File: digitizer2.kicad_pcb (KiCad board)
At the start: 6 copper layers, 4 parts, among them U1 XC7A35T, U2 FT2232H, U3 MT41J128M16, U4 ADS5403

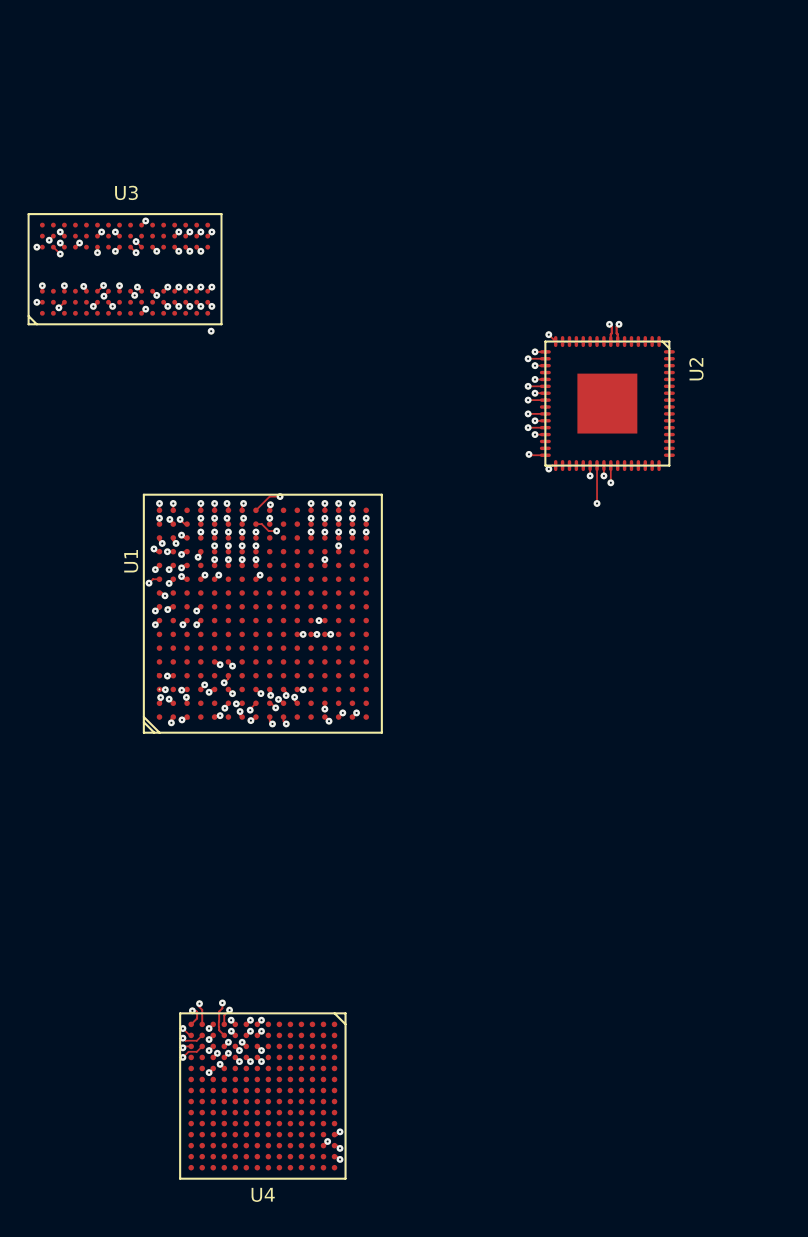
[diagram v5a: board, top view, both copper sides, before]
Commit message: Power supply initial selection
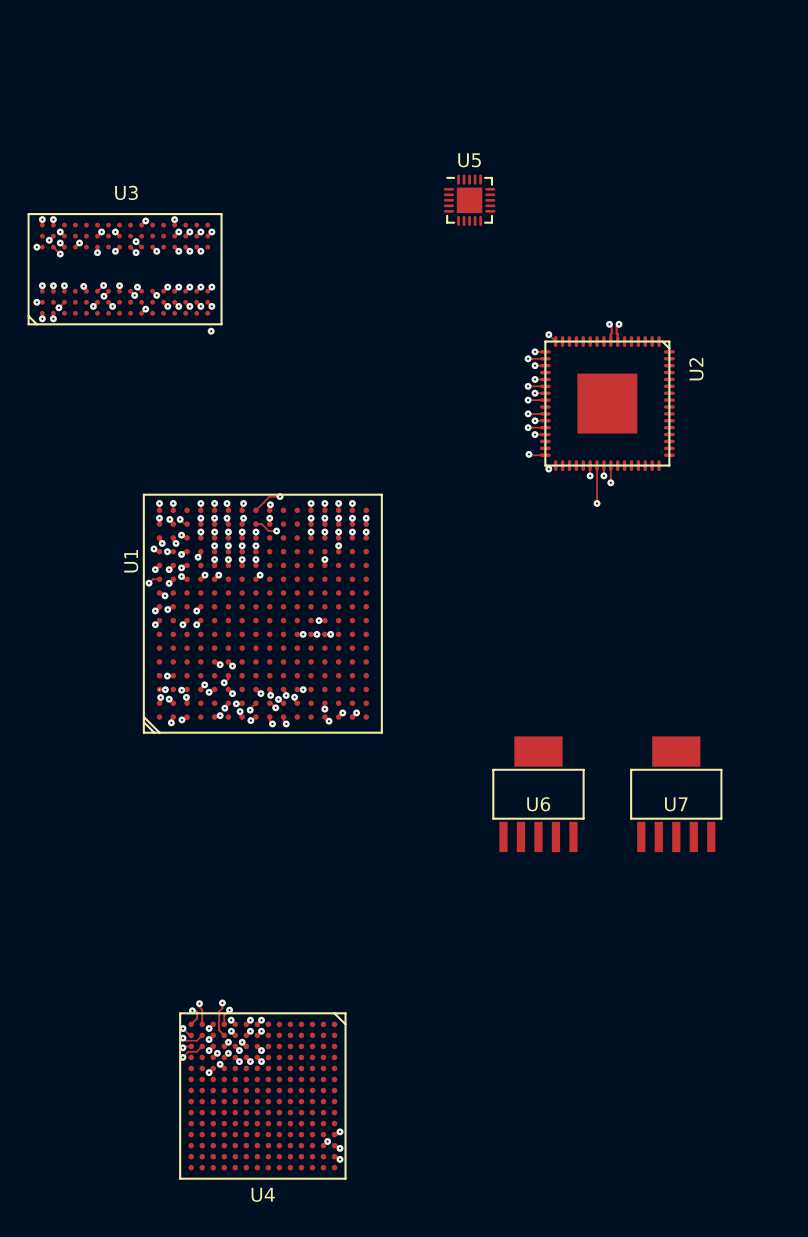
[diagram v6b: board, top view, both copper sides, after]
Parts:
- added U5: LTC3569, Housings_DFN_QFN:UQFN-20-1EP_3x3mm_Pitch0.4mm, F.Cu at (175.0, 65.0)
- added U6: TPS79618DCQ, digitizer2_modules:SOT-223-6, F.Cu at (180.0, 108.1)
- added U7: TPS79633DCQ, digitizer2_modules:SOT-223-6, F.Cu at (190.0, 108.1)
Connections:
- U1 pad A1: Net-(U1-PadA1) -> GND
- U1 pad A11: Net-(U1-PadA11) -> GND
- U1 pad B13: Net-(U1-PadB13) -> Net-(U1-PadA16)
- U1 pad B3: Net-(U1-PadB3) -> Net-(U1-PadA6)
- U1 pad B8: Net-(U1-PadB8) -> GND
- U1 pad C10: Net-(U1-PadC10) -> Net-(U1-PadA16)
- U1 pad C15: Net-(U1-PadC15) -> GND
- U1 pad C5: Net-(U1-PadC5) -> GND
- U1 pad D12: Net-(U1-PadD12) -> GND
- U1 pad D2: Net-(U1-PadD2) -> GND
- U1 pad D7: Net-(U1-PadD7) -> Net-(U1-PadA6)
- U1 pad E14: Net-(U1-PadE14) -> Net-(U1-PadA16)
- U1 pad E4: Net-(U1-PadE4) -> Net-(U1-PadA6)
- U1 pad E9: Net-(U1-PadE9) -> GND
- U1 pad F1: Net-(U1-PadF1) -> Net-(U1-PadA6)
- U1 pad F10: Net-(U1-PadF10) -> GND
- U1 pad F11: Net-(U1-PadF11) -> Net-(U1-PadE10)
- U1 pad F16: Net-(U1-PadF16) -> GND
- U1 pad F6: Net-(U1-PadF6) -> GND
- U1 pad F9: Net-(U1-PadF9) -> Net-(U1-PadF7)
- U1 pad G13: Net-(U1-PadG13) -> GND
- U1 pad G3: Net-(U1-PadG3) -> GND
- U1 pad G6: Net-(U1-PadG6) -> Net-(U1-PadF7)
- U1 pad G9: Net-(U1-PadG9) -> GND
- U1 pad H15: Net-(U1-PadH15) -> Net-(U1-PadA16)
- U1 pad H6: Net-(U1-PadH6) -> GND
- U1 pad H9: Net-(U1-PadH9) -> Net-(U1-PadF7)
- U1 pad J10: Net-(U1-PadJ10) -> Net-(U1-PadG10)
- U1 pad J11: Net-(U1-PadJ11) -> GND
- U1 pad J12: Net-(U1-PadJ12) -> Net-(U1-PadA16)
- U1 pad J2: Net-(U1-PadJ2) -> Net-(U1-PadA6)
- U1 pad J6: Net-(U1-PadJ6) -> Net-(U1-PadF7)
- U1 pad J9: Net-(U1-PadJ9) -> GND
- U1 pad K11: Net-(U1-PadK11) -> Net-(U1-PadG10)
- U1 pad K14: Net-(U1-PadK14) -> GND
- U1 pad K4: Net-(U1-PadK4) -> GND
- U1 pad K6: Net-(U1-PadK6) -> GND
- U1 pad K9: Net-(U1-PadK9) -> Net-(U1-PadF7)
- U1 pad L1: Net-(U1-PadL1) -> GND
- U1 pad L10: Net-(U1-PadL10) -> Net-(U1-PadG10)
- U1 pad L11: Net-(U1-PadL11) -> GND
- U1 pad L8: Net-(U1-PadL8) -> Net-(U1-PadF7)
- U1 pad M13: Net-(U1-PadM13) -> Net-(U1-PadL16)
- U1 pad M8: Net-(U1-PadM8) -> GND
- U1 pad N10: Net-(U1-PadN10) -> Net-(U1-PadL16)
- U1 pad N15: Net-(U1-PadN15) -> GND
- U1 pad N5: Net-(U1-PadN5) -> GND
- U1 pad P12: Net-(U1-PadP12) -> GND
- U1 pad P2: Net-(U1-PadP2) -> GND
- U1 pad P7: Net-(U1-PadP7) -> Net-(U1-PadL16)
- U1 pad R14: Net-(U1-PadR14) -> Net-(U1-PadL16)
- U1 pad R4: Net-(U1-PadR4) -> Net-(U1-PadM3)
- U1 pad R9: Net-(U1-PadR9) -> GND
- U1 pad T1: Net-(U1-PadT1) -> Net-(U1-PadM3)
- U1 pad T11: Net-(U1-PadT11) -> Net-(U1-PadL16)
- U1 pad T16: Net-(U1-PadT16) -> GND
- U1 pad T6: Net-(U1-PadT6) -> GND
- U2 pad 1: Net-(U2-Pad1) -> GND
- U2 pad 10: Net-(U2-Pad1) -> GND
- U2 pad 11: Net-(U2-Pad1) -> GND
- U2 pad 15: Net-(U2-Pad1) -> GND
- U2 pad 25: Net-(U2-Pad1) -> GND
- U2 pad 35: Net-(U2-Pad1) -> GND
- U2 pad 47: Net-(U2-Pad1) -> GND
- U2 pad 5: Net-(U2-Pad1) -> GND
- U2 pad 51: Net-(U2-Pad1) -> GND
- U2 pad PAD: Net-(U2-Pad1) -> GND
- U3 pad A9: Net-(U3-PadA9) -> GND
- U3 pad B1: Net-(U3-PadB1) -> GND
- U3 pad B3: Net-(U3-PadA9) -> GND
- U3 pad B9: Net-(U3-PadB1) -> GND
- U3 pad D1: Net-(U3-PadB1) -> GND
- U3 pad D8: Net-(U3-PadB1) -> GND
- U3 pad E1: Net-(U3-PadA9) -> GND
- U3 pad E2: Net-(U3-PadB1) -> GND
- U3 pad E8: Net-(U3-PadB1) -> GND
- U3 pad F9: Net-(U3-PadB1) -> GND
- U3 pad G1: Net-(U3-PadB1) -> GND
- U3 pad G8: Net-(U3-PadA9) -> GND
- U3 pad G9: Net-(U3-PadB1) -> GND
- U3 pad J2: Net-(U3-PadA9) -> GND
- U3 pad J8: Net-(U3-PadA9) -> GND
- U3 pad M1: Net-(U3-PadA9) -> GND
- U3 pad M9: Net-(U3-PadA9) -> GND
- U3 pad P1: Net-(U3-PadA9) -> GND
- U3 pad P9: Net-(U3-PadA9) -> GND
- U3 pad T1: Net-(U3-PadA9) -> GND
- U3 pad T9: Net-(U3-PadA9) -> GND
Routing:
- net GND: track 0.00 -> 4.60 mm, vias 0 -> 9
- net Net-(U1-PadA16): track 0.50 -> 3.06 mm, vias 1 -> 4
- net Net-(U1-PadH15): track 1.71 -> 0.00 mm, vias 1 -> 0
- net Net-(U1-PadA11): track 0.88 -> 0.00 mm, vias 1 -> 0
- net Net-(U1-PadC15): track 0.64 -> 0.00 mm, vias 1 -> 0
- net Net-(U1-PadJ2): track 0.57 -> 0.00 mm, vias 1 -> 0
- net Net-(U1-PadA6): track 0.00 -> 0.57 mm, vias 0 -> 1
- net Net-(U1-PadF16): track 0.54 -> 0.00 mm, vias 1 -> 0
- net Net-(U1-PadB13): track 0.43 -> 0.00 mm, vias 1 -> 0
- net Net-(U1-PadR14): track 0.43 -> 0.00 mm, vias 1 -> 0
- net Net-(U1-PadL16): track 0.00 -> 0.43 mm, vias 0 -> 1
- net Net-(U1-PadE14): track 0.43 -> 0.00 mm, vias 1 -> 0
- net Net-(U1-PadN15): track 0.43 -> 0.00 mm, vias 1 -> 0
- net Net-(U1-PadG13): track 0.42 -> 0.00 mm, vias 1 -> 0
- net Net-(U3-PadB2): track 0.00 -> 0.40 mm, vias 0 -> 1
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
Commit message: Config bank. Power labels
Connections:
- net Net-(U1-PadK10) renamed /INIT_B
- net Net-(U1-PadL9) renamed /PROGRAM_B
- net Net-(U4-PadD12) renamed /VDD_ADC_3V3
- U1 pad A16: Net-(U1-PadA16) -> /VDD_DRAM_1V5
- U1 pad A6: Net-(U1-PadA6) -> /VDD_ADC_1V8
- U1 pad B13: Net-(U1-PadA16) -> /VDD_DRAM_1V5
- U1 pad B3: Net-(U1-PadA6) -> /VDD_ADC_1V8
- U1 pad C10: Net-(U1-PadA16) -> /VDD_DRAM_1V5
- U1 pad D7: Net-(U1-PadA6) -> /VDD_ADC_1V8
- U1 pad E10: Net-(U1-PadE10) -> /VDD_FPGA_1V0
- U1 pad E14: Net-(U1-PadA16) -> /VDD_DRAM_1V5
- U1 pad E4: Net-(U1-PadA6) -> /VDD_ADC_1V8
- U1 pad E7: Net-(U1-PadE7) -> /VDD_FPGA_3V3
- U1 pad F1: Net-(U1-PadA6) -> /VDD_ADC_1V8
- U1 pad F11: Net-(U1-PadE10) -> /VDD_FPGA_1V0
- U1 pad F7: Net-(U1-PadF7) -> /VDD_FPGA_1V0
- U1 pad F8: Net-(U1-PadF8) -> /VDD_FPGA_1V8
- U1 pad F9: Net-(U1-PadF7) -> /VDD_FPGA_1V0
- U1 pad G10: Net-(U1-PadG10) -> /VDD_FPGA_1V8
- U1 pad G6: Net-(U1-PadF7) -> /VDD_FPGA_1V0
- U1 pad G7: Net-(U1-PadG7) -> GND
- U1 pad G8: Net-(U1-PadG8) -> /VDD_FPGA_1V8
- U1 pad H15: Net-(U1-PadA16) -> /VDD_DRAM_1V5
- U1 pad H7: Net-(U1-PadH7) -> GND
- U1 pad H9: Net-(U1-PadF7) -> /VDD_FPGA_1V0
- U1 pad J10: Net-(U1-PadG10) -> /VDD_FPGA_1V8
- U1 pad J12: Net-(U1-PadA16) -> /VDD_DRAM_1V5
- U1 pad J2: Net-(U1-PadA6) -> /VDD_ADC_1V8
- U1 pad J6: Net-(U1-PadF7) -> /VDD_FPGA_1V0
- U1 pad K11: Net-(U1-PadG10) -> /VDD_FPGA_1V8
- U1 pad K7: Net-(U1-PadK7) -> GND
- U1 pad K8: Net-(U1-PadK8) -> GND
- U1 pad K9: Net-(U1-PadF7) -> /VDD_FPGA_1V0
- U1 pad L10: Net-(U1-PadG10) -> /VDD_FPGA_1V8
- U1 pad L16: Net-(U1-PadL16) -> /VDD_FPGA_3V3
- U1 pad L6: Net-(U1-PadL6) -> /VDD_FPGA_3V3
- U1 pad L8: Net-(U1-PadF7) -> /VDD_FPGA_1V0
- U1 pad M10: Net-(U1-PadM10) -> GND
- U1 pad M11: Net-(U1-PadM11) -> /VDD_FPGA_3V3
- U1 pad M13: Net-(U1-PadL16) -> /VDD_FPGA_3V3
- U1 pad M9: Net-(U1-PadM9) -> /VDD_FPGA_3V3
- U1 pad N10: Net-(U1-PadL16) -> /VDD_FPGA_3V3
- U1 pad P7: Net-(U1-PadL16) -> /VDD_FPGA_3V3
- U1 pad R14: Net-(U1-PadL16) -> /VDD_FPGA_3V3
- U1 pad T11: Net-(U1-PadL16) -> /VDD_FPGA_3V3
- U2 pad 12: Net-(U2-Pad12) -> /VDD_FTDI_1V8
- U2 pad 13: Net-(U2-Pad13) -> GND
- U2 pad 20: Net-(U2-Pad20) -> /VDD_FPGA_3V3
- U2 pad 30: Net-(U2-Pad20) -> /VDD_FPGA_3V3
- U2 pad 31: Net-(U2-Pad20) -> /VDD_FPGA_3V3
- U2 pad 37: Net-(U2-Pad12) -> /VDD_FTDI_1V8
- U2 pad 42: Net-(U2-Pad20) -> /VDD_FPGA_3V3
- U2 pad 49: Net-(U2-Pad49) -> /VDD_FTDI_1V8
- U2 pad 50: Net-(U2-Pad50) -> /VDD_FPGA_3V3
- U2 pad 56: Net-(U2-Pad20) -> /VDD_FPGA_3V3
- U2 pad 64: Net-(U2-Pad12) -> /VDD_FTDI_1V8
- U3 pad A1: Net-(U3-PadA1) -> /VDD_DRAM_1V5
- U3 pad A8: Net-(U3-PadA1) -> /VDD_DRAM_1V5
- U3 pad B2: Net-(U3-PadB2) -> /VDD_DRAM_1V5
- U3 pad C1: Net-(U3-PadA1) -> /VDD_DRAM_1V5
- U3 pad C9: Net-(U3-PadA1) -> /VDD_DRAM_1V5
- U3 pad D2: Net-(U3-PadA1) -> /VDD_DRAM_1V5
- U3 pad D3: /DRAM_DM1 -> GND
- U3 pad D9: Net-(U3-PadB2) -> /VDD_DRAM_1V5
- U3 pad E7: /DRAM_DM0 -> GND
- U3 pad E9: Net-(U3-PadA1) -> /VDD_DRAM_1V5
- U3 pad F1: Net-(U3-PadA1) -> /VDD_DRAM_1V5
- U3 pad G7: Net-(U3-PadB2) -> /VDD_DRAM_1V5
- U3 pad H2: Net-(U3-PadA1) -> /VDD_DRAM_1V5
- U3 pad H9: Net-(U3-PadA1) -> /VDD_DRAM_1V5
- U3 pad K2: Net-(U3-PadB2) -> /VDD_DRAM_1V5
- U3 pad K8: Net-(U3-PadB2) -> /VDD_DRAM_1V5
- U3 pad L2: /DRAM_CS -> GND
- U3 pad N1: Net-(U3-PadB2) -> /VDD_DRAM_1V5
- U3 pad N9: Net-(U3-PadB2) -> /VDD_DRAM_1V5
- U3 pad R1: Net-(U3-PadB2) -> /VDD_DRAM_1V5
- U3 pad R9: Net-(U3-PadB2) -> /VDD_DRAM_1V5
- U4 pad A8: Net-(U4-PadA8) -> /VDD_ADC_1V8
- U4 pad A9: Net-(U4-PadA8) -> /VDD_ADC_1V8
- U4 pad B8: Net-(U4-PadA8) -> /VDD_ADC_1V8
- U4 pad B9: Net-(U4-PadA8) -> /VDD_ADC_1V8
- U4 pad C6: Net-(U4-PadC6) -> /VDD_ADC_1V8
- U4 pad C7: Net-(U4-PadC6) -> /VDD_ADC_1V8
- U4 pad C8: Net-(U4-PadA8) -> /VDD_ADC_1V8
- U4 pad D10: Net-(U4-PadD10) -> /VDD_ADC_1V8
- U4 pad D11: Net-(U4-PadD10) -> /VDD_ADC_1V8
- U4 pad D6: Net-(U4-PadC6) -> /VDD_ADC_1V8
- U4 pad D7: Net-(U4-PadC6) -> /VDD_ADC_1V8
- U4 pad D8: Net-(U4-PadA8) -> /VDD_ADC_1V8
- U4 pad E11: Net-(U4-PadD10) -> /VDD_ADC_1V8
- U4 pad F11: Net-(U4-PadD10) -> /VDD_ADC_1V8
- U4 pad G11: Net-(U4-PadD10) -> /VDD_ADC_1V8
- U4 pad G14: Net-(U4-PadG14) -> /VDD_ADC_1V8
- U4 pad H11: Net-(U4-PadD10) -> /VDD_ADC_1V8
- U4 pad H14: Net-(U4-PadG14) -> /VDD_ADC_1V8
- U4 pad J11: Net-(U4-PadD10) -> /VDD_ADC_1V8
- U4 pad K11: Net-(U4-PadD10) -> /VDD_ADC_1V8
- U4 pad L10: Net-(U4-PadD10) -> /VDD_ADC_1V8
- U4 pad L11: Net-(U4-PadD10) -> /VDD_ADC_1V8
- U4 pad L6: Net-(U4-PadC6) -> /VDD_ADC_1V8
- U4 pad L7: Net-(U4-PadC6) -> /VDD_ADC_1V8
- U4 pad L8: Net-(U4-PadA8) -> /VDD_ADC_1V8
- U4 pad M6: Net-(U4-PadC6) -> /VDD_ADC_1V8
- U4 pad M7: Net-(U4-PadC6) -> /VDD_ADC_1V8
- U4 pad M8: Net-(U4-PadA8) -> /VDD_ADC_1V8
- U4 pad N11: Net-(U4-PadD10) -> /VDD_ADC_1V8
- U4 pad N8: Net-(U4-PadA8) -> /VDD_ADC_1V8
- U4 pad P11: Net-(U4-PadD10) -> /VDD_ADC_1V8
- U4 pad P8: Net-(U4-PadA8) -> /VDD_ADC_1V8
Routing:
- net /VDD_DRAM_1V5: track 0.00 -> 3.86 mm, vias 0 -> 6
- net Net-(U1-PadA16): track 3.06 -> 0.00 mm, vias 4 -> 0
- net Net-(U1-PadA6): track 0.57 -> 0.00 mm, vias 1 -> 0
- net /VDD_ADC_1V8: track 0.00 -> 0.57 mm, vias 0 -> 1
- net Net-(U1-PadL16): track 0.43 -> 0.00 mm, vias 1 -> 0
- net /VDD_FPGA_3V3: track 0.00 -> 0.43 mm, vias 0 -> 1
- net Net-(U3-PadB2): track 0.40 -> 0.00 mm, vias 1 -> 0
- net Net-(U3-PadA1): track 0.40 -> 0.00 mm, vias 1 -> 0

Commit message: Cleanup. Add Eeprom.
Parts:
- added U8: 93LC46BT-I/OT, digitizer2_modules:SOT-23-6, F.Cu at (195.0, 80.0)
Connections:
- U1 pad J8: Net-(U1-PadJ8) -> GND
- U1 pad L15: Net-(U1-PadL15) -> GND
